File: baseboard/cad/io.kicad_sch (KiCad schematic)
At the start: 29 parts, among them J1 DC POWER JACK, J2 1/4" JACK, STEREO, J23 2P_HEADER, J24 2P_HEADER, J25 2P_HEADER, J26 2P_HEADER, J3 6-440054-2, J4 6-440129-2, J5 1/4" JACK, STEREO

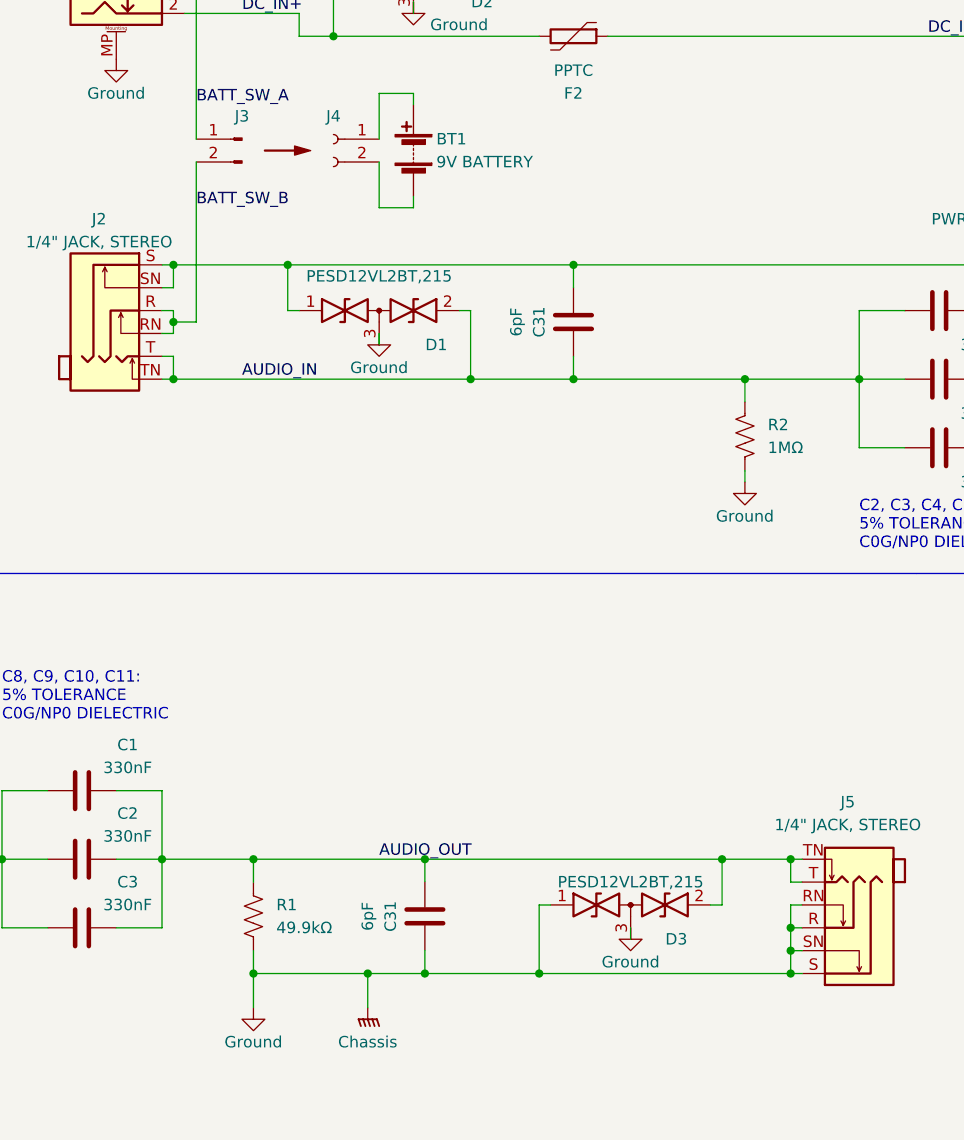
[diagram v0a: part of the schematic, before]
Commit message: cleaning up layout, added graphic symbols
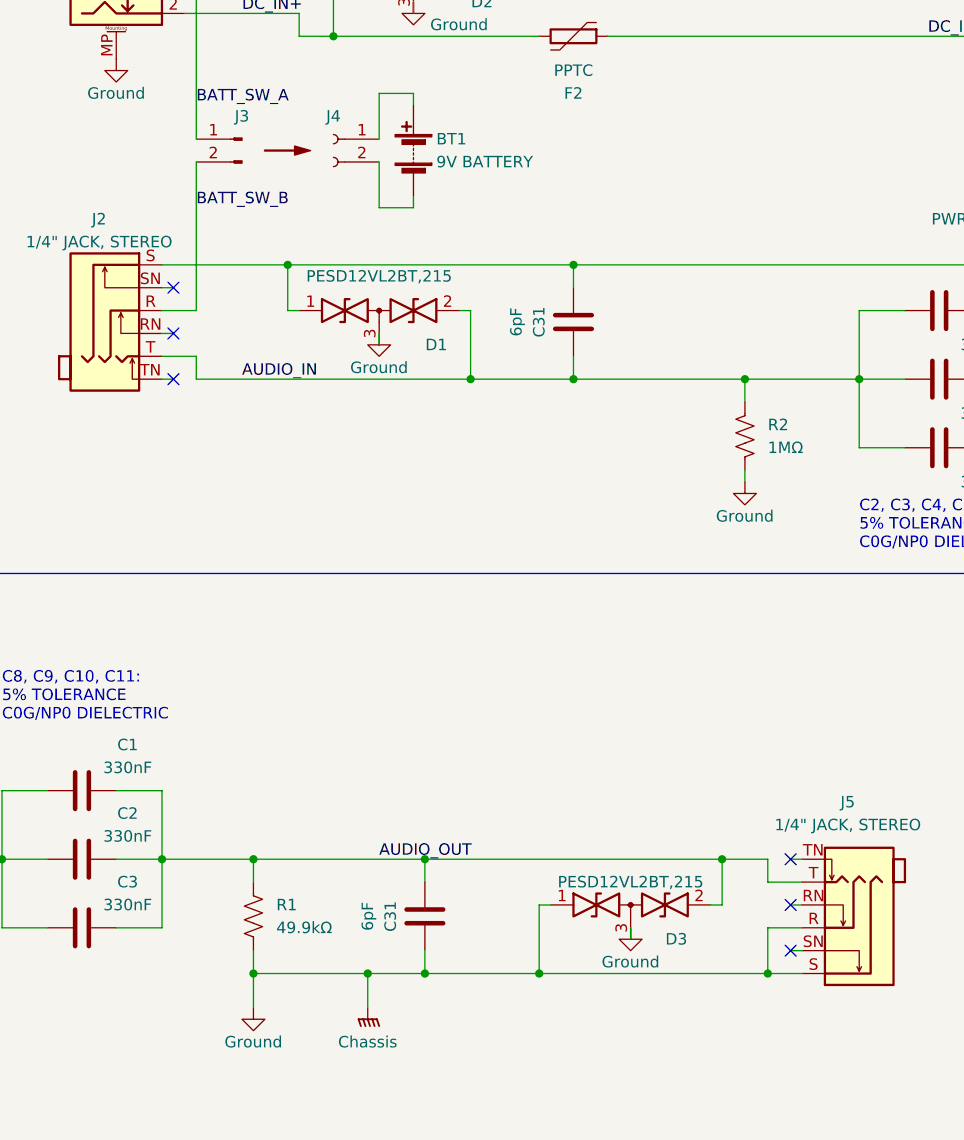
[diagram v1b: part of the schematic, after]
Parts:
- renumbered G1 to CHS1
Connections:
- net AUDIO_IN: no longer J2.TN
- net AUDIO_OUT: no longer J5.TN
- net BATT_SW_B: no longer J2.RN
- net GND: no longer J2.SN, J5.RN, J5.SN
- no-connect marks 0 -> 6
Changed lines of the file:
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@@
     (comment 9 "5: PCB LAYOUT ACCORDING TO DATASHEET FOR ALL COMPONENTS")
   )
-  (junction (at 57.15 80.01) (diameter 0) (color 0 0 0 0)
-  )
   (junction (at 146.05 73.66) (diameter 0) (color 0 0 0 0)
   )
@@
   (junction (at 151.13 86.36) (diameter 0) (color 0 0 0 0)
   )
-  (junction (at 57.15 86.36) (diameter 0) (color 0 0 0 0)
+  (junction (at 123.19 152.4) (diameter 0) (color 0 0 0 0)
   )
   (junction (at 212.09 35.56) (diameter 0) (color 0 0 0 0)
@@
   (junction (at 199.39 35.56) (diameter 0) (color 0 0 0 0)
   )
-  (junction (at 125.73 152.4) (diameter 0) (color 0 0 0 0)
-  )
-  (junction (at 57.15 73.66) (diameter 0) (color 0 0 0 0)
-  )
   (junction (at 162.56 35.56) (diameter 0) (color 0 0 0 0)
   )
   (junction (at 85.09 139.7) (diameter 0) (color 0 0 0 0)
   )
-  (junction (at 125.73 149.86) (diameter 0) (color 0 0 0 0)
-  )
   (junction (at 101.6 86.36) (diameter 0) (color 0 0 0 0)
   )
@@
   (junction (at 120.65 86.36) (diameter 0) (color 0 0 0 0)
   )
-  (junction (at 125.73 139.7) (diameter 0) (color 0 0 0 0)
-  )
   (junction (at 133.35 86.36) (diameter 0) (color 0 0 0 0)
   )
@@
   (junction (at 93.98 38.1) (diameter 0) (color 0 0 0 0)
   )
-  (junction (at 125.73 147.32) (diameter 0) (color 0 0 0 0)
-  )
   (junction (at 101.6 73.66) (diameter 0) (color 0 0 0 0)
   )
@@
   (junction (at 55.88 139.7) (diameter 0) (color 0 0 0 0)
   )
+  (no_connect (at 57.15 81.28))
+  (no_connect (at 57.15 76.2))
+  (no_connect (at 57.15 86.36))
+  (no_connect (at 125.73 149.86))
+  (no_connect (at 125.73 144.78))
+  (no_connect (at 125.73 139.7))
   (wire (pts (xy 55.88 147.32) (xy 50.8 147.32))
     (stroke (width 0) (type default))
@@
     (stroke (width 0) (type default))
   )
-  (wire (pts (xy 59.69 62.23) (xy 59.69 80.01))
+  (wire (pts (xy 59.69 62.23) (xy 59.69 78.74))
     (stroke (width 0) (type default))
   )
@@
     (stroke (width 0) (type default))
   )
-  (wire (pts (xy 57.15 86.36) (xy 57.15 83.82))
-    (stroke (width 0) (type default))
-  )
-  (wire (pts (xy 57.15 80.01) (xy 59.69 80.01))
+  (wire (pts (xy 55.88 78.74) (xy 59.69 78.74))
     (stroke (width 0) (type default))
   )
@@
     (stroke (width 0) (type default))
   )
-  (wire (pts (xy 57.15 73.66) (xy 57.15 76.2))
-    (stroke (width 0) (type default))
-  )
   (wire (pts (xy 71.12 78.74) (xy 69.85 78.74))
     (stroke (width 0) (type default))
@@
     (stroke (width 0) (type default))
   )
-  (wire (pts (xy 57.15 86.36) (xy 90.17 86.36))
-    (stroke (width 0) (type default))
-  )
   (wire (pts (xy 228.6 158.75) (xy 220.98 158.75))
     (stroke (width 0) (type default))
   )
+  (wire (pts (xy 59.69 86.36) (xy 90.17 86.36))
+    (stroke (width 0) (type default))
+  )
   (wire (pts (xy 85.09 152.4) (xy 85.09 149.86))
     (stroke (width 0) (type default))
@@
     (stroke (width 0) (type default))
   )
-  (wire (pts (xy 57.15 78.74) (xy 57.15 80.01))
-    (stroke (width 0) (type default))
-  )
   (polyline (pts (xy 139.7 107.95) (xy 254 107.95))
     (stroke (width 0) (type default))
@@
     (stroke (width 0) (type default))
   )
-  (wire (pts (xy 125.73 147.32) (xy 127 147.32))
+  (wire (pts (xy 123.19 147.32) (xy 127 147.32))
     (stroke (width 0) (type default))
   )
@@
     (stroke (width 0) (type default))
   )
-  (wire (pts (xy 57.15 81.28) (xy 57.15 80.01))
-    (stroke (width 0) (type default))
-  )
   (wire (pts (xy 199.39 35.56) (xy 212.09 35.56))
     (stroke (width 0) (type default))
   )
-  (wire (pts (xy 125.73 142.24) (xy 125.73 139.7))
+  (wire (pts (xy 123.19 142.24) (xy 123.19 139.7))
     (stroke (width 0) (type default))
   )
@@
     (stroke (width 0) (type default))
   )
-  (wire (pts (xy 125.73 149.86) (xy 125.73 152.4))
+  (wire (pts (xy 55.88 86.36) (xy 57.15 86.36))
     (stroke (width 0) (type default))
   )
@@
     (stroke (width 0) (type default))
   )
-  (wire (pts (xy 55.88 86.36) (xy 57.15 86.36))
-    (stroke (width 0) (type default))
-  )
   (wire (pts (xy 83.82 54.61) (xy 80.01 54.61))
     (stroke (width 0) (type default))
@@
     (stroke (width 0) (type default))
   )
-  (wire (pts (xy 55.88 83.82) (xy 57.15 83.82))
+  (wire (pts (xy 55.88 83.82) (xy 59.69 83.82))
     (stroke (width 0) (type default))
   )
@@
     (stroke (width 0) (type default))
   )
-  (wire (pts (xy 55.88 73.66) (xy 57.15 73.66))
+  (wire (pts (xy 55.88 73.66) (xy 69.85 73.66))
     (stroke (width 0) (type default))
   )
@@
     (stroke (width 0) (type default))
   )
-  (wire (pts (xy 118.11 139.7) (xy 125.73 139.7))
+  (wire (pts (xy 118.11 139.7) (xy 123.19 139.7))
     (stroke (width 0) (type default))
   )
@@
     (stroke (width 0) (type default))
   )
+  (wire (pts (xy 59.69 83.82) (xy 59.69 86.36))
+    (stroke (width 0) (type default))
+  )
+  (wire (pts (xy 123.19 152.4) (xy 127 152.4))
+    (stroke (width 0) (type default))
+  )
   (wire (pts (xy 101.6 86.36) (xy 120.65 86.36))
     (stroke (width 0) (type default))
@@
     (stroke (width 0) (type default))
   )
-  (wire (pts (xy 125.73 139.7) (xy 127 139.7))
-    (stroke (width 0) (type default))
-  )
   (wire (pts (xy 69.85 73.66) (xy 69.85 78.74))
     (stroke (width 0) (type default))
@@
     (stroke (width 0) (type default))
   )
-  (wire (pts (xy 125.73 152.4) (xy 127 152.4))
-    (stroke (width 0) (type default))
-  )
   (wire (pts (xy 66.04 152.4) (xy 66.04 156.21))
     (stroke (width 0) (type default))
@@
     (stroke (width 0) (type default))
   )
+  (wire (pts (xy 127 139.7) (xy 125.73 139.7))
+    (stroke (width 0) (type default))
+  )
   (wire (pts (xy 93.98 38.1) (xy 97.79 38.1))
     (stroke (width 0) (type default))
@@
     (stroke (width 0) (type default))
   )
-  (wire (pts (xy 127 142.24) (xy 125.73 142.24))
+  (wire (pts (xy 127 142.24) (xy 123.19 142.24))
     (stroke (width 0) (type default))
   )
@@
     (stroke (width 0) (type default))
   )
-  (wire (pts (xy 55.88 78.74) (xy 57.15 78.74))
-    (stroke (width 0) (type default))
-  )
-  (wire (pts (xy 57.15 73.66) (xy 69.85 73.66))
-    (stroke (width 0) (type default))
-  )
   (wire (pts (xy 151.13 93.98) (xy 146.05 93.98))
     (stroke (width 0) (type default))
@@
     (stroke (width 0) (type default))
   )
-  (wire (pts (xy 125.73 144.78) (xy 125.73 147.32))
-    (stroke (width 0) (type default))
-  )
   (wire (pts (xy 118.11 144.78) (xy 118.11 139.7))
     (stroke (width 0) (type default))
@@
     (stroke (width 0) (type default))
   )
+  (wire (pts (xy 123.19 147.32) (xy 123.19 152.4))
+    (stroke (width 0) (type default))
+  )
   (wire (pts (xy 177.8 127) (xy 185.42 127))
     (stroke (width 0) (type default))
@@
     (stroke (width 0) (type default))
   )
-  (wire (pts (xy 97.79 152.4) (xy 125.73 152.4))
+  (wire (pts (xy 97.79 152.4) (xy 123.19 152.4))
     (stroke (width 0) (type default))
   )
   (wire (pts (xy 101.6 73.66) (xy 101.6 76.2))
-    (stroke (width 0) (type default))
-  )
-  (wire (pts (xy 125.73 147.32) (xy 125.73 149.86))
     (stroke (width 0) (type default))
   )
@@
     )
   )
-  (netclass_flag "" (length 2.54) (shape round) (at 119.38 139.7 180) (fields_autoplaced)
-    (effects (font (size 1.27 1.27)) (justify right bottom))
-    (property "Audio" "Audio" (at 120.0785 142.24 0)
+  (netclass_flag "" (length 2.54) (shape round) (at 111.76 139.7 0) (fields_autoplaced)
+    (effects (font (size 1.27 1.27)) (justify left bottom))
+    (property "Audio" "Audio" (at 112.4585 137.16 0)
       (effects (font (size 1.27 1.27) italic) (justify left))
     )
@@
   (symbol (lib_id "Library:Chassis") (at 78.74 156.21 0) (mirror y) (unit 1)
     (in_bom yes) (on_board yes) (dnp no)
-    (property "Reference" "G1" (at 78.74 161.29 0)
+    (property "Reference" "CHS1" (at 78.74 161.29 0)
       (effects (font (size 1.27 1.27)) hide)
     )
@@
       (project "1590N1 IO Board"
         (path "/190888c1-6ce2-4681-a836-dc477e444e49/e436358c-d730-4540-92b5-b7475a7c4a63"
-          (reference "G1") (unit 1)
-        )
-      )
+          (reference "CHS1") (unit 1)
+        )
+      )
